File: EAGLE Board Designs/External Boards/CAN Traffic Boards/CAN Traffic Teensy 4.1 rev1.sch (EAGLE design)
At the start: 7 parts, among them X1 CONNECTOR-4NANO-FIT_RIGHT_ANG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

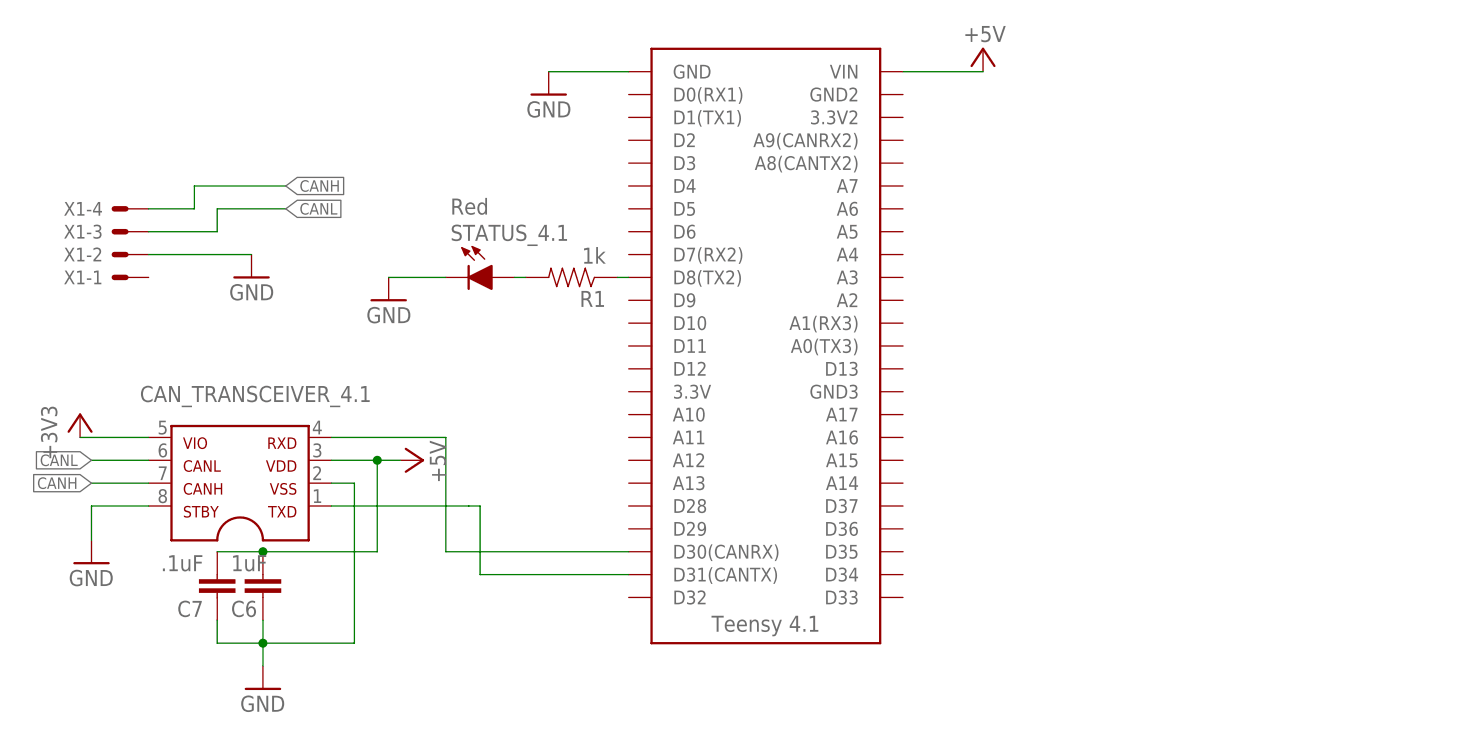
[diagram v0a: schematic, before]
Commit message: CAN Transceiver Boards
Added CAN Termination resistors, remade boards, added labels, put all LEDs on the same pin, added silksreens, and switched LED packages.
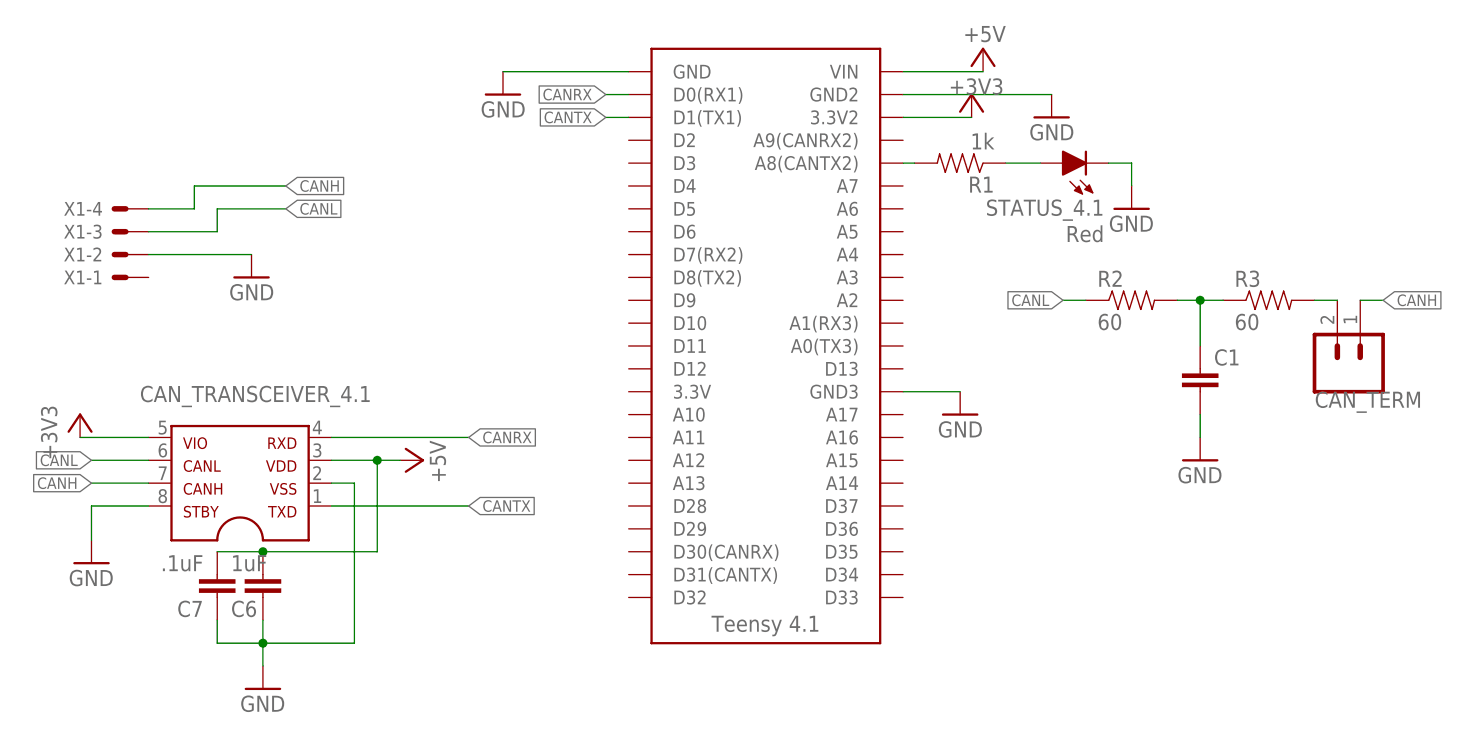
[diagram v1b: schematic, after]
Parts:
- added C1: (no value), HyTechDevices:CAP0603-CAP
- added CAN_TERM: M02_SLIM, HyTechDevices:M02_SLIM
- added R2, R3: 60, HyTechDevices:RESISTOR0603-RES
- STATUS_4.1: device HyTechDevices:LED-0805 -> HyTechDevices:LED-0603
- renumbered U$2 to 4.1
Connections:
- removed net N$4: 4.1.D8(TX2), R1.1
- new net CANRX: 4.1.D0(RX1), CAN_TRANSCEIVER_4.1.4
- new net CANTX: 4.1.D1(TX1), CAN_TRANSCEIVER_4.1.1
- new net N$6: CAN_TERM.2, R3.2
- net +3V3: now also 4.1.3.3V2
- net CANH: now also CAN_TERM.1
- net CANL: now also R2.1
- net GND: now also 4.1.GND2, 4.1.GND3, C1.2
- net N$1: now also 4.1.A8(CANTX2), R1.2; no longer 4.1.D30(CANRX), CAN_TRANSCEIVER_4.1.4
- net N$2: now also R1.1, STATUS_4.1.A; no longer 4.1.D31(CANTX), CAN_TRANSCEIVER_4.1.1
- net N$3: now also C1.1, R2.2, R3.1; no longer R1.2, STATUS_4.1.A
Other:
- moved on the sheet: R1, STATUS_4.1
